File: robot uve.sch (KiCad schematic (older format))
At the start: 59 parts, among them J1 pulsador1, J10 HC-SR04, J11 HC-SR04, J12 HC-SR04, J13 TB_1X3, J14 I2C_B, J15 I2C_C, J16 NeoPixel, J17 neopixel, J18 +5V IN, J19 GND, J2 I2C_A, J20 pulsador2, J21 IR, J3 TB_1X3, J4 comunicacion a rpi, J5 12V IN, J6 GND, J7 HC-SR04, J8 HC-SR04, J9 HC-SR04, K1 RELAY_C, K3 RELAY_C, P1 Digital, P10 CONN_01X01, P11 CONN_01X01, P12 CONN_01X01, P13 CONN_01X01, P14 motor3, P15 motor2, P16 Sensores de Linea, P17 motor1, P18 motor4, P2 Power, P3 Analog, P4 Analog, P5 PWM, P6 PWM, P7 Communication, P8 CONN_01X01, P9 CONN_01X01, Q1 2N7002, Q3 2N7002, Q4 2N7002

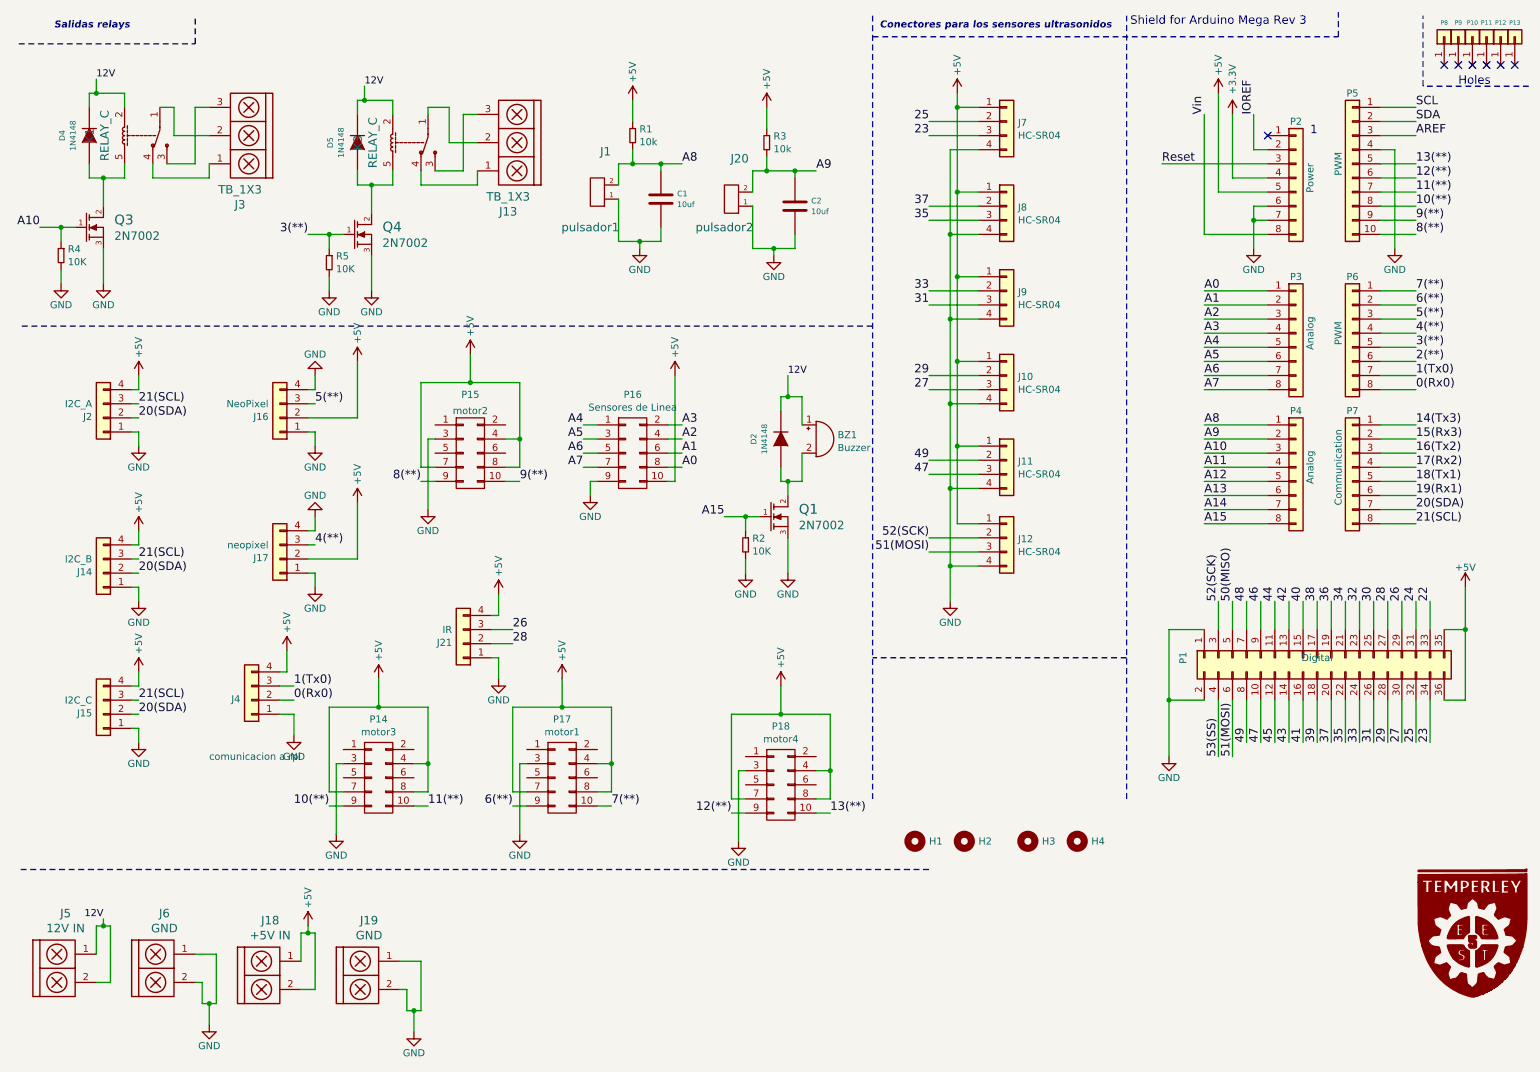
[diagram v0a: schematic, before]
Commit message: modificacion en el pcb
se modifico el pcb
se agrego boton reset
se modifico seregrafia
se modifico vias
y se agrego archicos BOM
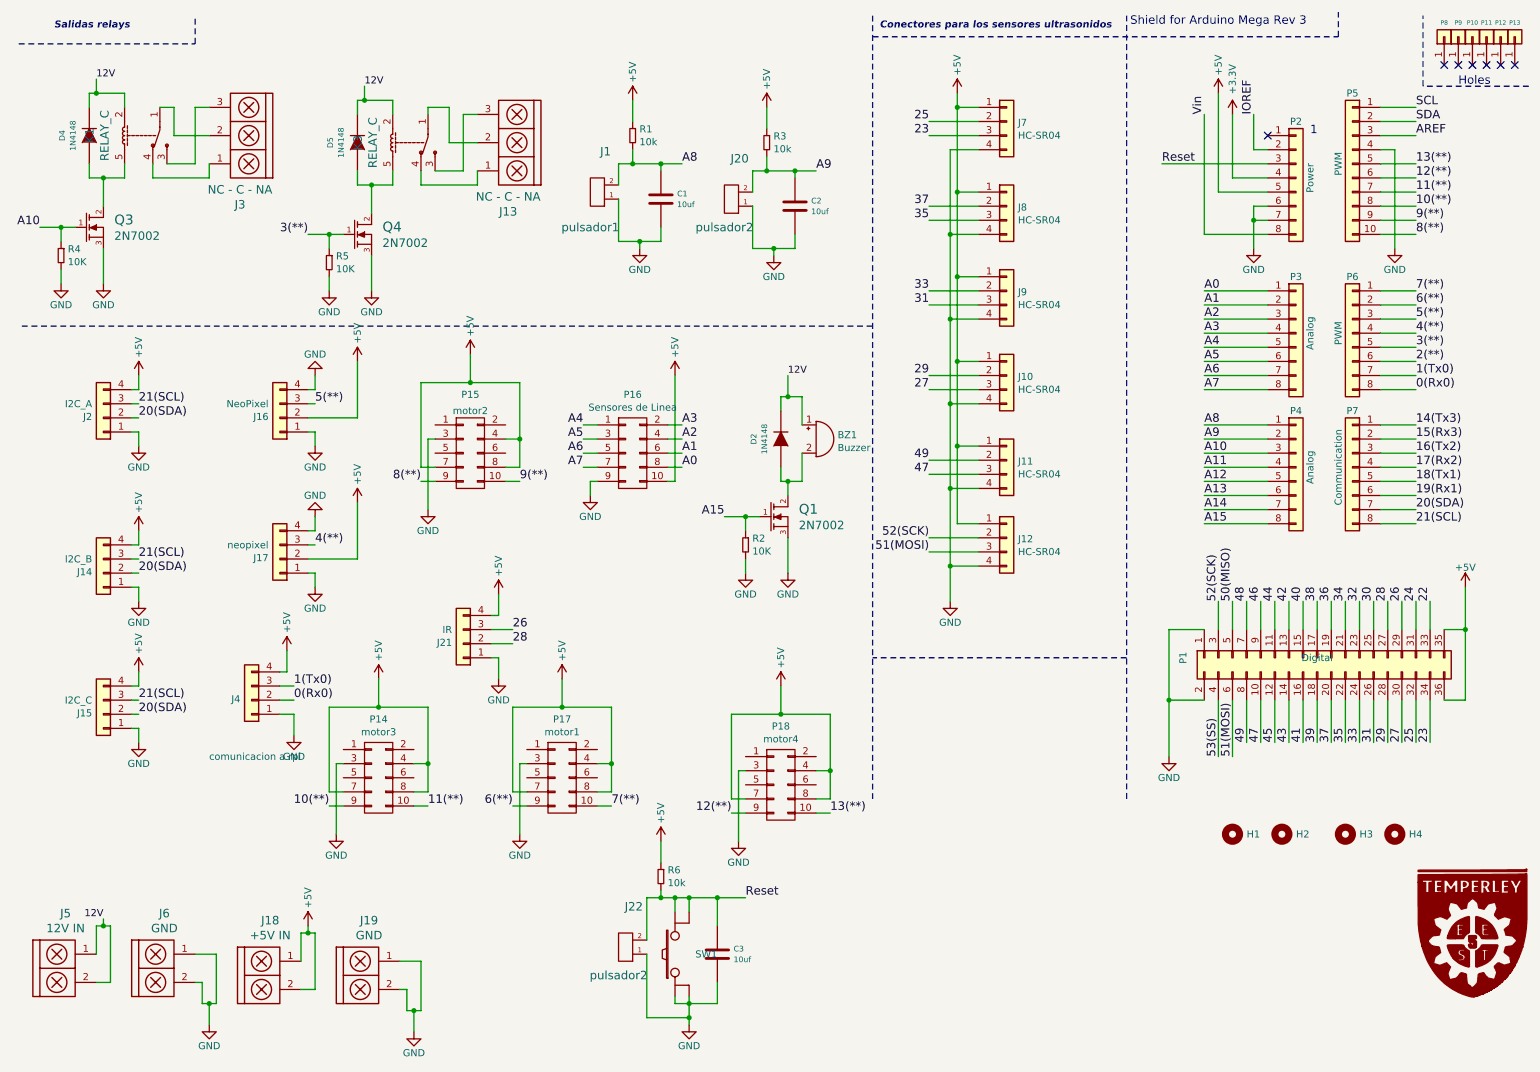
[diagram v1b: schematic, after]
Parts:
- added C3: 10uf, EESTN5:CAP_ELEC_5x11mm, symbol EESTN5:C
- added J22: pulsador2, EESTN5:Pin_Header_2, symbol EESTN5:HEADER_2
- added R6: 10k, EESTN5:RES0.3, symbol EESTN5:R
- added SW1: SW_PUSH, EESTN5:Pulsador_TH_4, symbol EESTN5:SW_PUSH
- J13, J3: value TB_1X3 -> NC - C - NA
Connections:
- net +5V: now also R6.1
- net GND: now also C3.2, J22.1, SW1.1, SW1.2
- net Reset: now also C3.1, J22.2, R6.2, SW1.3, SW1.4
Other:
- moved on the sheet: H1, H2, H3, H4
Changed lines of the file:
@@
 P 4100 1500
 F 0 "J13" H 4232 1889 60  0000 C CNN
-F 1 "TB_1X3" H 4232 1783 60  0000 C CNN
+F 1 "NC - C - NA" H 4232 1783 60  0000 C CNN
 F 2 "EESTN5:BORNERA3_AZUL" H 4050 1550 60  0001 C CNN
 F 3 "" H 4050 1550 60  0000 C CNN
@@
 P 2200 1450
 F 0 "J3" H 2332 1839 60  0000 C CNN
-F 1 "TB_1X3" H 2332 1733 60  0000 C CNN
+F 1 "NC - C - NA" H 2332 1733 60  0000 C CNN
 F 2 "EESTN5:BORNERA3_AZUL" H 2150 1500 60  0001 C CNN
 F 3 "" H 2150 1500 60  0000 C CNN
@@
 Wire Notes Line
 	6550 500  6550 6050
-Wire Notes Line
-	6950 6550 500  6550
 $Comp
 L EESTN5:LOGO_EESTN5_2 #G1
@@
 L EESTN5:Mounting_Hole H1
 U 1 1 5D4C8887
-P 6850 6350
-F 0 "H1" H 6950 6350 50  0000 L CNN
-F 1 "Mounting_Hole" H 6850 6475 50  0001 C CNN
-F 2 "EESTN5:hole_3mm" H 6850 6350 60  0001 C CNN
-F 3 "" H 6850 6350 60  0001 C CNN
-	1    6850 6350
+P 9100 6300
+F 0 "H1" H 9200 6300 50  0000 L CNN
+F 1 "Mounting_Hole" H 9100 6425 50  0001 C CNN
+F 2 "EESTN5:hole_3mm" H 9100 6300 60  0001 C CNN
+F 3 "" H 9100 6300 60  0001 C CNN
+	1    9100 6300
 	1    0    0    -1
 $EndComp
@@
 L EESTN5:Mounting_Hole H2
 U 1 1 5D4C9FF8
-P 7200 6350
-F 0 "H2" H 7300 6350 50  0000 L CNN
-F 1 "Mounting_Hole" H 7200 6475 50  0001 C CNN
-F 2 "EESTN5:hole_3mm" H 7200 6350 60  0001 C CNN
-F 3 "" H 7200 6350 60  0001 C CNN
-	1    7200 6350
+P 9450 6300
+F 0 "H2" H 9550 6300 50  0000 L CNN
+F 1 "Mounting_Hole" H 9450 6425 50  0001 C CNN
+F 2 "EESTN5:hole_3mm" H 9450 6300 60  0001 C CNN
+F 3 "" H 9450 6300 60  0001 C CNN
+	1    9450 6300
 	1    0    0    -1
 $EndComp
@@
 L EESTN5:Mounting_Hole H3
 U 1 1 5D4CADFF
-P 7650 6350
-F 0 "H3" H 7750 6350 50  0000 L CNN
-F 1 "Mounting_Hole" H 7650 6475 50  0001 C CNN
-F 2 "EESTN5:hole_3mm" H 7650 6350 60  0001 C CNN
-F 3 "" H 7650 6350 60  0001 C CNN
-	1    7650 6350
+P 9900 6300
+F 0 "H3" H 10000 6300 50  0000 L CNN
+F 1 "Mounting_Hole" H 9900 6425 50  0001 C CNN
+F 2 "EESTN5:hole_3mm" H 9900 6300 60  0001 C CNN
+F 3 "" H 9900 6300 60  0001 C CNN
+	1    9900 6300
 	1    0    0    -1
 $EndComp
@@
 L EESTN5:Mounting_Hole H4
 U 1 1 5D4CAE09
-P 8000 6350
-F 0 "H4" H 8100 6350 50  0000 L CNN
-F 1 "Mounting_Hole" H 8000 6475 50  0001 C CNN
-F 2 "EESTN5:hole_3mm" H 8000 6350 60  0001 C CNN
-F 3 "" H 8000 6350 60  0001 C CNN
-	1    8000 6350
+P 10250 6300
+F 0 "H4" H 10350 6300 50  0000 L CNN
+F 1 "Mounting_Hole" H 10250 6425 50  0001 C CNN
+F 2 "EESTN5:hole_3mm" H 10250 6300 60  0001 C CNN
+F 3 "" H 10250 6300 60  0001 C CNN
+	1    10250 6300
 	1    0    0    -1
 $EndComp
@@
 Text Label 4000 4950 0    60   ~ 0
 28
+$Comp
+L EESTN5:HEADER_2 J22
+U 1 1 5FC803BD
+P 4850 7100
+F 0 "J22" H 4842 6813 60  0000 C CNN
+F 1 "pulsador2" H 4950 7300 60  0000 C CNN
+F 2 "EESTN5:Pin_Header_2" H 4850 7350 60  0001 C CNN
+F 3 "" H 4850 7350 60  0000 C CNN
+	1    4850 7100
+	-1   0    0    1
+$EndComp
+$Comp
+L EESTN5:R R6
+U 1 1 5FC8080B
+P 5050 6600
+F 0 "R6" H 5098 6646 50  0000 L CNN
+F 1 "10k" H 5098 6555 50  0000 L CNN
+F 2 "EESTN5:RES0.3" H 5050 6600 60  0001 C CNN
+F 3 "" H 5050 6600 60  0000 C CNN
+	1    5050 6600
+	1    0    0    -1
+$EndComp
+$Comp
+L EESTN5:C C3
+U 1 1 5FC80815
+P 5450 7150
+F 0 "C3" H 5565 7188 40  0000 L CNN
+F 1 "10uf" H 5565 7112 40  0000 L CNN
+F 2 "EESTN5:CAP_ELEC_5x11mm" H 5488 7000 30  0001 C CNN
+F 3 "" H 5450 7150 60  0000 C CNN
+	1    5450 7150
+	1    0    0    -1
+$EndComp
+$Comp
+L robot-uve-rescue:GND-power #PWR0142
+U 1 1 5FC8082B
+P 5250 7650
+F 0 "#PWR0142" H 5250 7400 50  0001 C CNN
+F 1 "GND" H 5250 7500 50  0000 C CNN
+F 2 "" H 5250 7650 50  0000 C CNN
+F 3 "" H 5250 7650 50  0000 C CNN
+	1    5250 7650
+	1    0    0    -1
+$EndComp
+$Comp
+L robot-uve-rescue:+5V-power #PWR0143
+U 1 1 5FC80838
+P 5050 6350
+F 0 "#PWR0143" H 5050 6200 50  0001 C CNN
+F 1 "+5V" V 5050 6550 50  0000 C CNN
+F 2 "" H 5050 6350 50  0000 C CNN
+F 3 "" H 5050 6350 50  0000 C CNN
+	1    5050 6350
+	1    0    0    -1
+$EndComp
+Text Label 5650 6750 0    60   ~ 0
+Reset
+$Comp
+L EESTN5:SW_PUSH SW1
+U 1 1 5FCE883F
+P 5150 7150
+F 0 "SW1" V 5150 7006 50  0000 R CNN
+F 1 "SW_PUSH" H 5150 7070 50  0001 C CNN
+F 2 "EESTN5:Pulsador_TH_4" H 5150 7150 60  0001 C CNN
+F 3 "" H 5150 7150 60  0000 C CNN
+	1    5150 7150
+	0    -1   -1   0
+$EndComp
+Wire Wire Line
+	5250 6850 5250 6750
+Wire Wire Line
+	5250 6750 5150 6750
+Wire Wire Line
+	4950 6750 4950 7050
+Wire Wire Line
+	4950 7150 4950 7600
+Wire Wire Line
+	4950 7600 5250 7600
+Wire Wire Line
+	5250 7600 5250 7500
+Wire Wire Line
+	5150 7500 5250 7500
+Connection ~ 5250 7500
+Wire Wire Line
+	5250 7500 5250 7450
+Wire Wire Line
+	5150 7500 5150 7450
+Wire Wire Line
+	5150 6850 5150 6750
+Connection ~ 5150 6750
+Wire Wire Line
+	5150 6750 5050 6750
+Wire Wire Line
+	5050 6700 5050 6750
+Connection ~ 5050 6750
+Wire Wire Line
+	5050 6750 4950 6750
+Wire Wire Line
+	5050 6350 5050 6500
+Wire Wire Line
+	5450 6950 5450 6750
+Wire Wire Line
+	5450 6750 5250 6750
+Connection ~ 5250 6750
+Wire Wire Line
+	5250 7500 5450 7500
+Wire Wire Line
+	5450 7500 5450 7350
+Wire Wire Line
+	5250 7600 5250 7650
+Connection ~ 5250 7600
+Wire Wire Line
+	5450 6750 5650 6750
+Connection ~ 5450 6750
 $EndSCHEMATC

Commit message: Varios
Pase a SMD (1206) las resistencias.
Modifique una conexión a 5V para evitar un jumper.
Acomode un poco más la serigrafia (todavía falta).
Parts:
- R1, R3, R6: footprint EESTN5:RES0.3 -> EESTN5:R_1206
- R2, R4, R5: footprint EESTN5:RES0.2 -> EESTN5:R_1206
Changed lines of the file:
@@
 F 0 "R2" H 5698 4296 50  0000 L CNN
 F 1 "10K" H 5698 4205 50  0000 L CNN
-F 2 "EESTN5:RES0.2" H 5650 4250 60  0001 C CNN
+F 2 "EESTN5:R_1206" H 5650 4250 60  0001 C CNN
 F 3 "" H 5650 4250 60  0000 C CNN
 	1    5650 4250
@@
 F 0 "R5" H 2748 2296 50  0000 L CNN
 F 1 "10K" H 2748 2205 50  0000 L CNN
-F 2 "EESTN5:RES0.2" H 2700 2250 60  0001 C CNN
+F 2 "EESTN5:R_1206" H 2700 2250 60  0001 C CNN
 F 3 "" H 2700 2250 60  0000 C CNN
 	1    2700 2250
@@
 F 0 "R4" H 848 2246 50  0000 L CNN
 F 1 "10K" H 848 2155 50  0000 L CNN
-F 2 "EESTN5:RES0.2" H 800 2200 60  0001 C CNN
+F 2 "EESTN5:R_1206" H 800 2200 60  0001 C CNN
 F 3 "" H 800 2200 60  0000 C CNN
 	1    800  2200
@@
 F 0 "R1" H 4898 1396 50  0000 L CNN
 F 1 "10k" H 4898 1305 50  0000 L CNN
-F 2 "EESTN5:RES0.3" H 4850 1350 60  0001 C CNN
+F 2 "EESTN5:R_1206" H 4850 1350 60  0001 C CNN
 F 3 "" H 4850 1350 60  0000 C CNN
 	1    4850 1350
@@
 F 0 "R3" H 5848 1446 50  0000 L CNN
 F 1 "10k" H 5848 1355 50  0000 L CNN
-F 2 "EESTN5:RES0.3" H 5800 1400 60  0001 C CNN
+F 2 "EESTN5:R_1206" H 5800 1400 60  0001 C CNN
 F 3 "" H 5800 1400 60  0000 C CNN
 	1    5800 1400
@@
 F 0 "R6" H 5098 6646 50  0000 L CNN
 F 1 "10k" H 5098 6555 50  0000 L CNN
-F 2 "EESTN5:RES0.3" H 5050 6600 60  0001 C CNN
+F 2 "EESTN5:R_1206" H 5050 6600 60  0001 C CNN
 F 3 "" H 5050 6600 60  0000 C CNN
 	1    5050 6600
